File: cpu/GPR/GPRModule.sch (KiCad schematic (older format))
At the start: 58 parts, among them J1 Interconnect B, J2 Interconnect A, U1 74LS173, U10 74LS245, U11 74LS245, U12 74LS245, U2 74LS173, U3 74LS173, U4 74LS173, U5 74LS245, U6 74LS245, U7 74LS245, U8 74LS245, U9 74LS245

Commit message: Lots of changes
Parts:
- removed U1, U2, U3, U4: 74LS173, Package_SO:SOIC-16_3.9x9.9mm_P1.27mm, symbol 74xx:74LS173
- added C13: 0.1uF, Capacitor_SMD:C_0603_1608Metric_Pad1.05x0.95mm_HandSolder, symbol Device:C
- added D16, D17, D18, D19: LED_AMBER, LED_SMD:LED_1206_3216Metric_Pad1.42x1.75mm_HandSolder, symbol Device:LED_ALT
- added R16, R17, R18, R19: 220R, Resistor_SMD:R_0603_1608Metric_Pad1.05x0.95mm_HandSolder, symbol Device:R
- added U1, U2: 74HCT574, Package_SO:SOIC-20W_7.5x12.8mm_P1.27mm, symbol 74xx:74HCT574
- added U13: 74LS126, Package_SO:SOIC-14_3.9x8.7mm_P1.27mm, symbol 74xx:74LS126
- added U3: 74LS14, Package_SO:SOIC-14_3.9x8.7mm_P1.27mm, symbol 74xx:74LS14
- D0, D1, D10, D11, D12, D13, D14, D15, D2, D3, D4, D5, D6, D7, D8, D9: value LED_ALT -> LED_RED
- J1: renamed from J2; value Interconnect A -> Interconnect 1
- J2: renamed from J1; value Interconnect B -> Interconnect 2
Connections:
- net labels added: d_bus_00, d_bus_01, d_bus_02, d_bus_03, d_bus_04, d_bus_05, d_bus_06, d_bus_07, d_bus_08, d_bus_09, d_bus_10, d_bus_11, d_bus_12, d_bus_13, d_bus_14, d_bus_15, d_bus_read, d_bus_write, x_bus_00, x_bus_01, x_bus_02, x_bus_03, x_bus_04, x_bus_05, x_bus_06, x_bus_07, x_bus_08, x_bus_09, x_bus_10, x_bus_11, x_bus_12, x_bus_13, x_bus_14, x_bus_15, x_bus_write, y_bus_00, y_bus_01, y_bus_02, y_bus_03, y_bus_04, y_bus_05, y_bus_06, y_bus_07, y_bus_08, y_bus_09, y_bus_10, y_bus_11, y_bus_12, y_bus_13, y_bus_14, y_bus_15, y_bus_write, ~DBG, ~d_bus_write, ~x_bus_write, ~y_bus_write
- net labels removed: DBG, a1bus_00, a1bus_01, a1bus_02, a1bus_03, a1bus_04, a1bus_05, a1bus_06, a1bus_07, a1bus_08, a1bus_09, a1bus_10, a1bus_11, a1bus_12, a1bus_13, a1bus_14, a1bus_15, a1bus_write, a2bus_00, a2bus_01, a2bus_02, a2bus_03, a2bus_04, a2bus_05, a2bus_06, a2bus_07, a2bus_08, a2bus_09, a2bus_10, a2bus_11, a2bus_12, a2bus_13, a2bus_14, a2bus_15, a2bus_write, dbus_00, dbus_01, dbus_02, dbus_03, dbus_04, dbus_05, dbus_06, dbus_07, dbus_08, dbus_09, dbus_10, dbus_11, dbus_12, dbus_13, dbus_14, dbus_15, dbus_read, dbus_write
- wire segments 590 -> 563
- no-connect marks 6 -> 17
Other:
- note added: "XBUS Buffer"
- note added: "YBUS Buffer"
- note removed: "A1BUS Buffer"
- note removed: "A2BUS Buffer"
- moved on the sheet: C1, C10, C11, C12, C2, C3, C4, C5, C6, C7, C8, C9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

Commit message: Completed GPR 1.2 PCB and started lots of other things. * Started ALU * Updated Constant Reg * Completed v1.2 GPR * Added random symbols * Updated Memory * Updated plots
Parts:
- removed C12, C13: 0.1uF, Capacitor_SMD:C_0603_1608Metric_Pad1.05x0.95mm_HandSolder, symbol Device:C
- removed J1: Interconnect 1, Connector_PinHeader_2.54mm:PinHeader_2x17_P2.54mm_Horizontal, symbol Connector_Generic:Conn_02x17_Odd_Even
- removed J2: Interconnect 2, Connector_PinHeader_2.54mm:PinHeader_2x17_P2.54mm_Horizontal, symbol Connector_Generic:Conn_02x17_Odd_Even
- removed R0, R1, R10, R11, R12, R13, R14, R15, R2, R3, R4, R5, R6, R7, R8, R9: 220R, Resistor_SMD:R_0603_1608Metric_Pad1.05x0.95mm_HandSolder, symbol Device:R
- removed U10, U11, U12, U5, U6, U7, U8, U9: 74LS245, Package_SO:SOIC-20W_7.5x12.8mm_P1.27mm, symbol 74xx:74LS245
- removed U3: 74LS14, Package_SO:SOIC-14_3.9x8.7mm_P1.27mm, symbol 74xx:74LS14
- added J1: Interconnect, Connector_PCBEdge:BUS_PCI, symbol cpu_custom_symbols:Bus_PCI_32bit_5V
- added RN1, RN2: 220R, Resistor_SMD:R_Array_Convex_8x0602, symbol Device:R_Pack08
- added U10, U3, U4, U5, U6, U7, U8, U9: 74LS245, Package_SO:SOIC-20W_7.5x12.8mm_P1.27mm, symbol cpu_custom_symbols:74LS245_BiDirection
- added unit 5 of U11
- renumbered U13 to U11
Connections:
- net labels removed: CLK, HLT, RST, d_bus_write, x_bus_write, y_bus_write, ~CLK
- wire segments 563 -> 374
- no-connect marks 17 -> 63
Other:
- moved on the sheet: C1, C10, C11, C2, C3, C4, C5, C6, C7, C8, C9, D0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

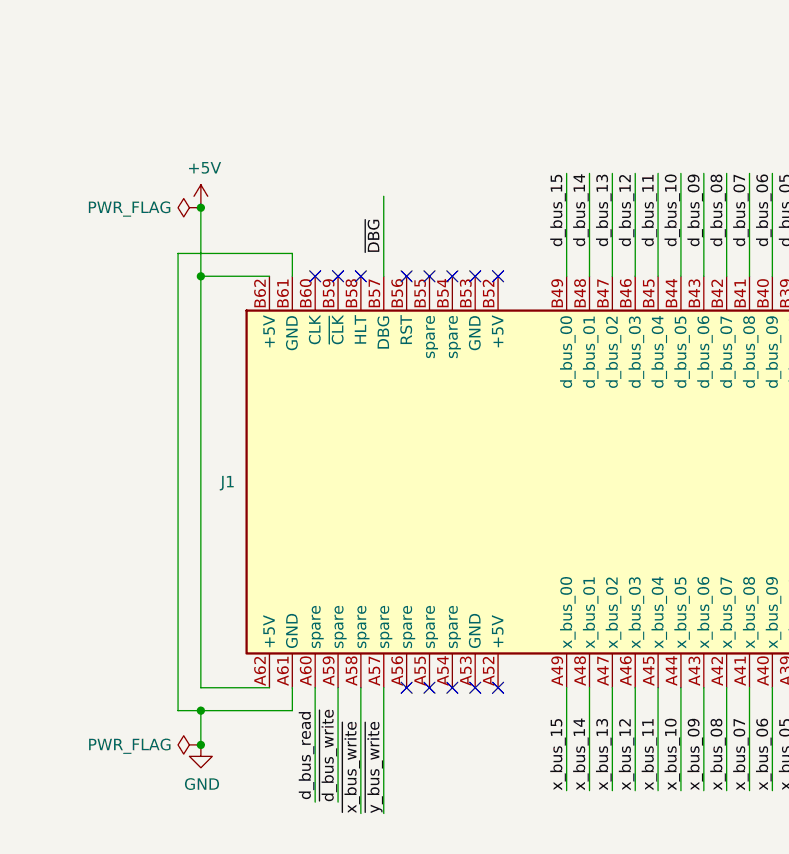
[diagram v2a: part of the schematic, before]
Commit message: Added missing power pins to GPR
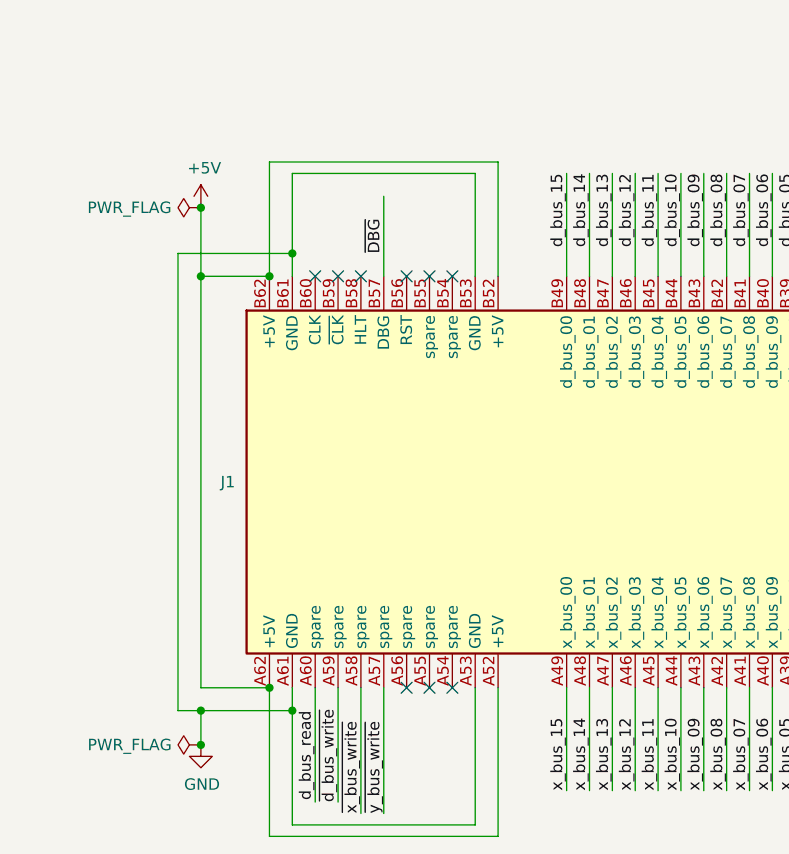
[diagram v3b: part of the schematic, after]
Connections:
- net +5V: now also J1.A52 (+5V), J1.B52 (+5V)
- net GND: now also J1.A53 (GND), J1.B53 (GND)
- no-connect marks 63 -> 59
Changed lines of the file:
@@
 NoConn ~ 3150 7650
 NoConn ~ 3250 7650
-NoConn ~ 3450 7650
-NoConn ~ 3350 7650
 NoConn ~ 5350 7650
 NoConn ~ 5450 7650
@@
 NoConn ~ 3150 9450
 NoConn ~ 3250 9450
-NoConn ~ 3350 9450
-NoConn ~ 3450 9450
 Wire Wire Line
 	10650 9950 11150 9950
@@
 Wire Wire Line
 	11150 9100 11150 9950
+Wire Wire Line
+	3350 7650 3350 7200
+Wire Wire Line
+	3350 7200 2550 7200
+Wire Wire Line
+	2550 7200 2550 7550
+Connection ~ 2550 7550
+Wire Wire Line
+	3450 7650 3450 7150
+Wire Wire Line
+	3450 7150 2450 7150
+Wire Wire Line
+	2450 7150 2450 7650
+Connection ~ 2450 7650
+Wire Wire Line
+	3350 9450 3350 10050
+Wire Wire Line
+	3350 10050 2550 10050
+Wire Wire Line
+	2550 10050 2550 9550
+Connection ~ 2550 9550
+Wire Wire Line
+	3450 9450 3450 10100
+Wire Wire Line
+	3450 10100 2450 10100
+Wire Wire Line
+	2450 10100 2450 9450
+Connection ~ 2450 9450
 $EndSCHEMATC

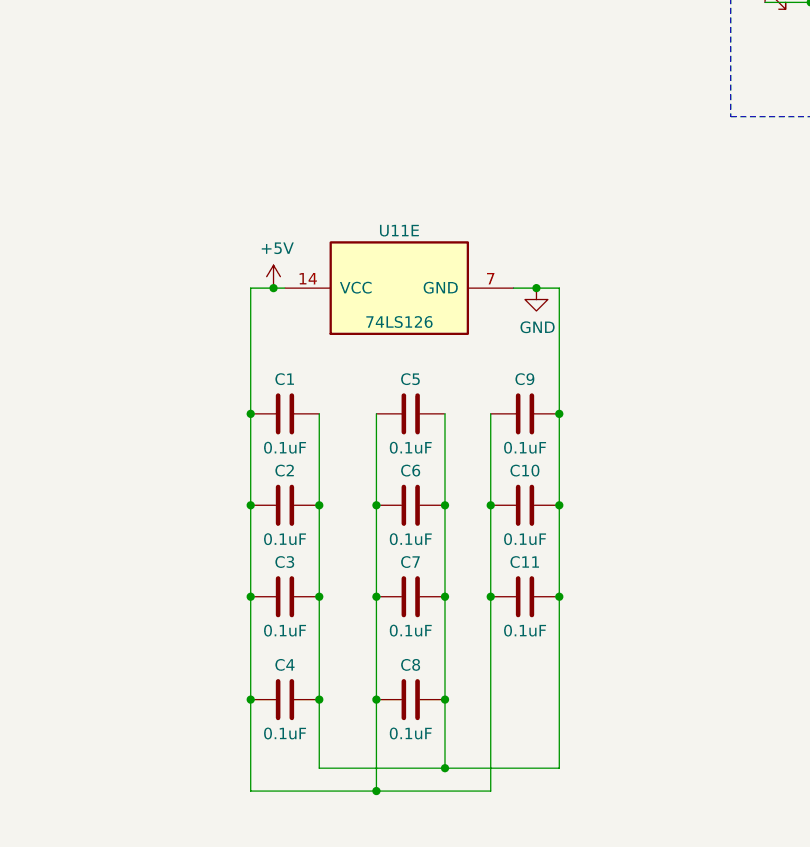
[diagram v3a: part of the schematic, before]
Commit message: Added 10uF caps to GPR
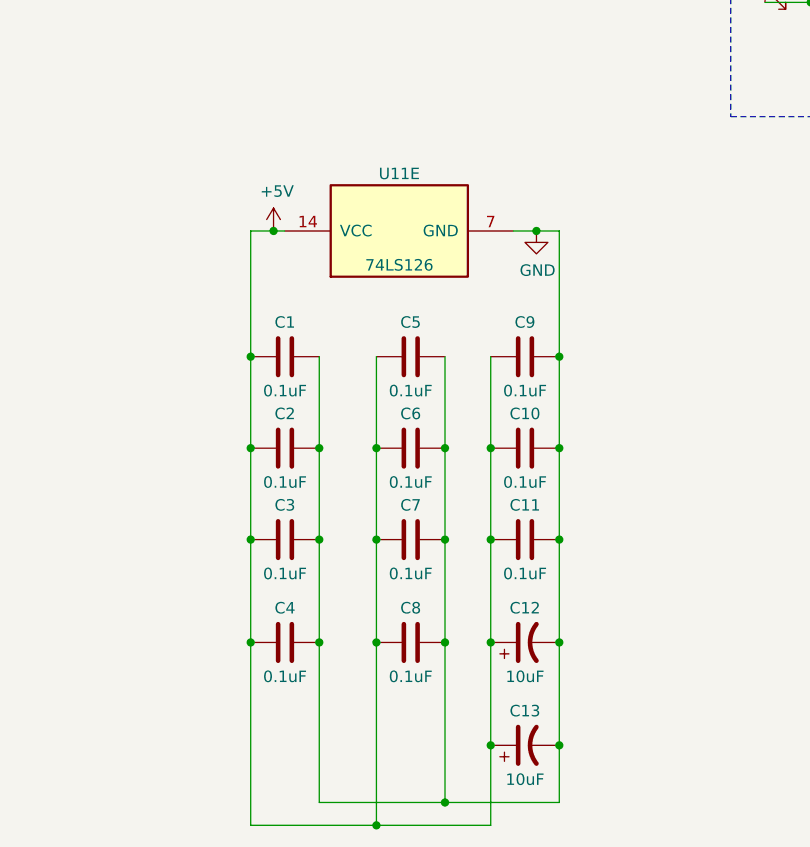
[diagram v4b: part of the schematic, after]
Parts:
- added C12, C13: 10uF, Capacitor_SMD:CP_Elec_4x5.4, symbol Device:CP1
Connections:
- net +5V: now also C12.1, C13.1
- net GND: now also C12.2, C13.2
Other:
- moved on the sheet: C1, C10, C11, C2, C3, C4, C5, C6, C7, C8, C9, U11E
